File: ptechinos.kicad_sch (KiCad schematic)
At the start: 76 parts, among them J1 B+, J2 Battery, J3 B-, J4 TRRS, J5 Trackpad FPC, J6 OLED, J7 Pogo, SW1 SW_Power, SW2 Reset, U1 ProMicro

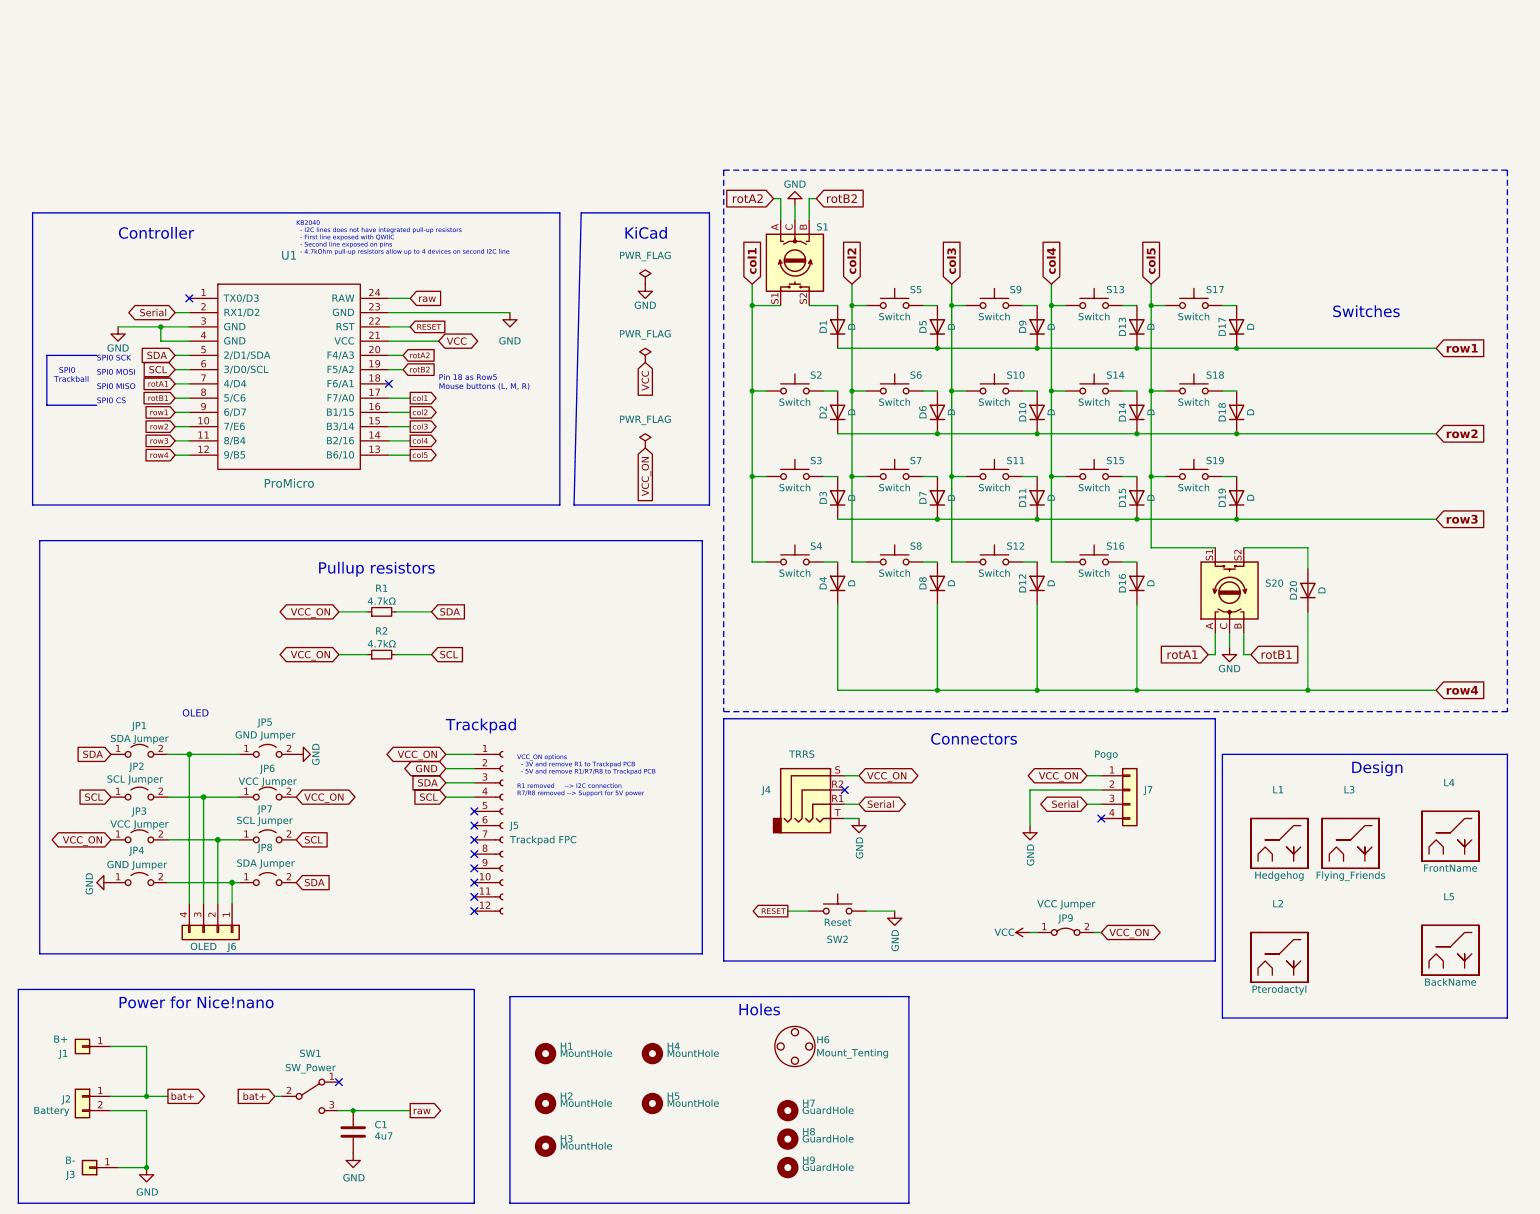
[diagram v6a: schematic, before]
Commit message: ✨ ♻️ - Add footprint for pogo connectors. Add SPI header pins 1.27mm pitch (used for trackball component). Update I2C resistors position (now below the MCU board on the other side). Replace reset switch with a smaller one and put it below the pogo connector (solder on the opposite side). Rename VCC / VCC_ON to 3.3V to make it more explicit about the voltage used by the RP2040 (does not break compatibility with EliteC like board). Remove VCC_ON altogether to make routing cleaner / easier.
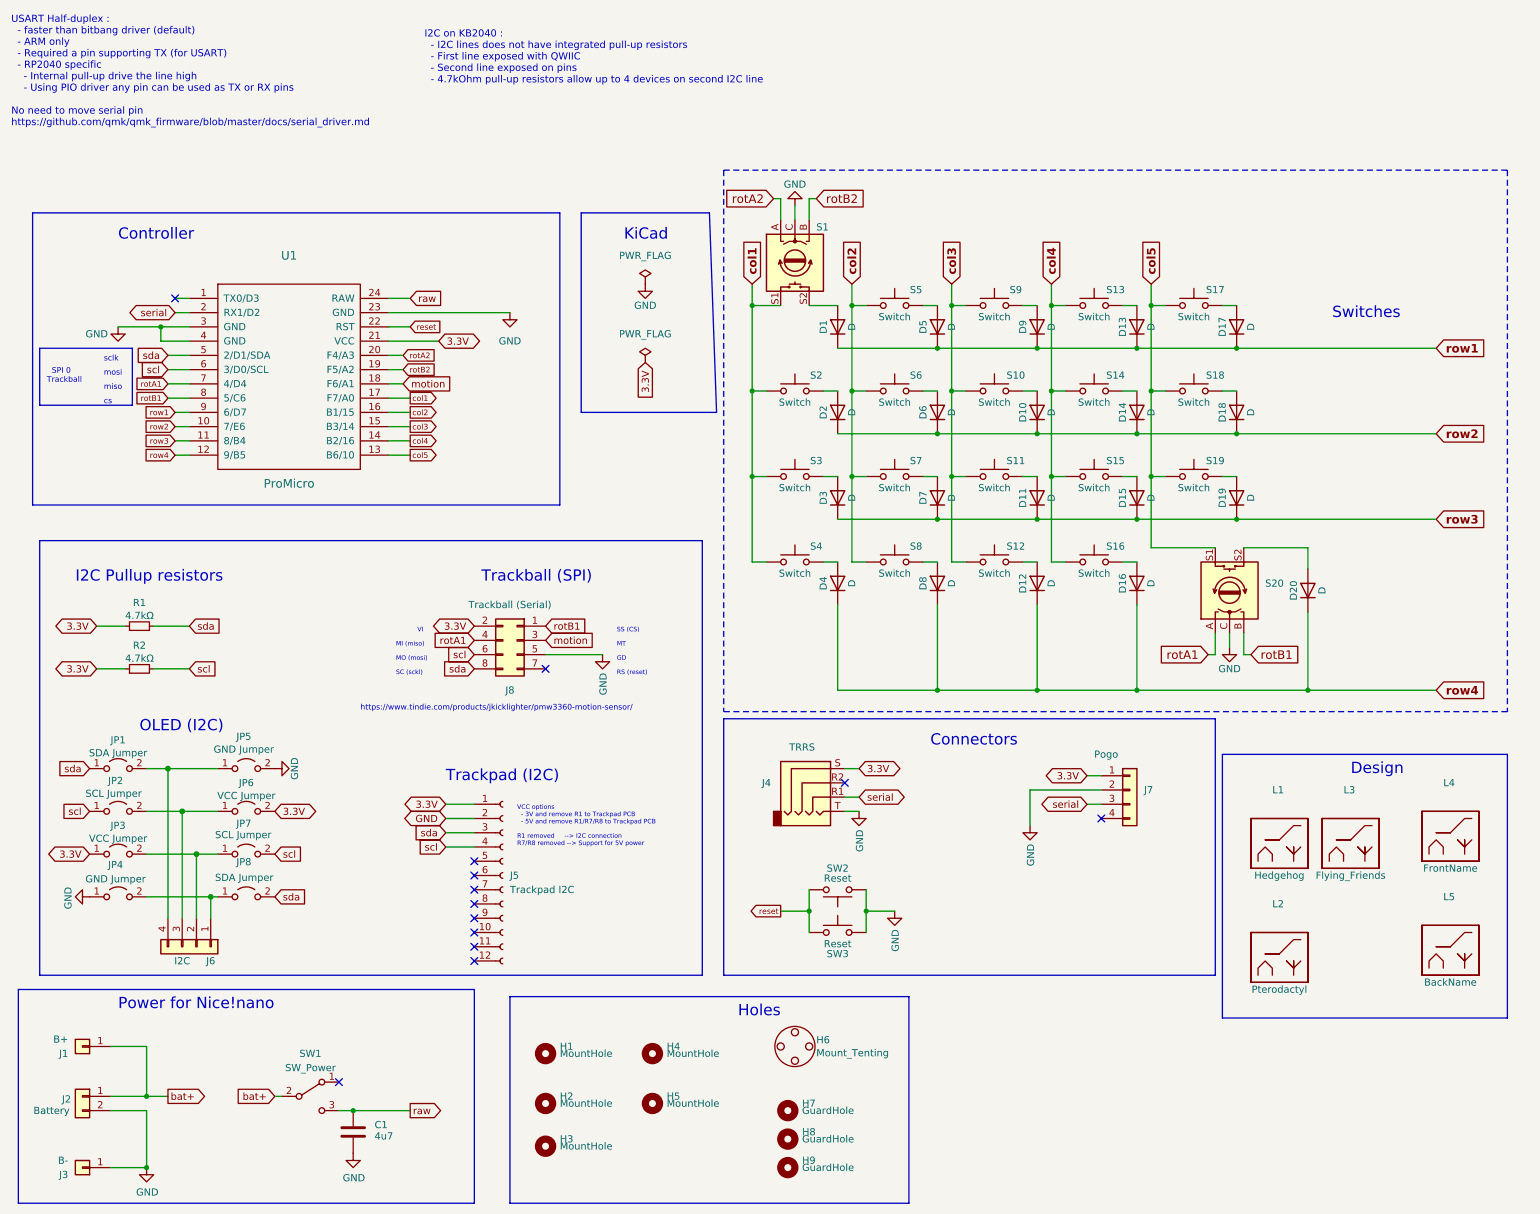
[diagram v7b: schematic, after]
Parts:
- removed JP9: VCC Jumper, Jumper:SolderJumper-2_P1.3mm_Bridged_RoundedPad1.0x1.5mm, symbol Jumper:Jumper_2_Bridged
- added J8: Trackball (Serial), Connector_PinHeader_1.27mm:PinHeader_2x04_P1.27mm_Horizontal, symbol Connector_Generic:Conn_02x04_Odd_Even
- added SW3: Reset, ptechinos:SW_SKRKAEE020_ALPS, symbol Switch:SW_Push
- J1, J3: footprint ptechinos:1pin_conn -> ptechinos:PinHeader_1x01
- J5: value Trackpad FPC -> Trackpad I2C
- J6: value OLED -> I2C
- J7: footprint ptechinos:PinSocket_1x04_P2.54mm_Vertical -> Connector_PinHeader_2.54mm:PinHeader_1x04_P2.54mm_Vertical
- SW2: footprint ptechinos:TACT_SWITCH_TVBP06 -> ptechinos:SW_SKRKAEE020_ALPS
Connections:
- net VCC_ON is gone; now on net 3.3V: J4.S, J5.1 (Pin_1), J7.1 (Pin_1), JP3.1 (A), JP6.2 (B), R1.1, R2.1
- net GND: now also SW2.1, J8.5 (Pin_5), SW3.2; no longer SW2.2
- net rotA1: now also J8.4 (Pin_4)
- net rotB1: now also J8.1 (Pin_1)
- net motion: now reaches U1.18 (F6/A1)
- net motion: now also J8.3 (Pin_3)
- net RESET renamed reset
- net reset: now also SW2.2, SW3.1; no longer SW2.1
- net SCL renamed scl
- net scl: now also J8.6 (Pin_6)
- net SDA renamed sda
- net sda: now also J8.8 (Pin_8)
- net Serial renamed serial
- net VCC renamed 3.3V
- net 3.3V: now also J8.2 (Pin_2)
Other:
- note added: "GD"
- note added: "I2C Pullup resistors"
- note added: "I2C on KB2040 : - I2C lines does not have integrated pull-up resistors - First line exposed with QWIIC - Second line exposed on pins - 4.7kOhm pull-up resistors allow up to 4 devices on second I2C line"
- note added: "MI (miso)"
- note added: "MO (mosi)"
- note added: "MT"
- note added: "OLED (I2C)"
- note added: "RS (reset)"
- note added: "SC (sckl)"
- note added: "SPI 0 Trackball"
- note added: "SS (CS)"
- note added: "Trackball (SPI)"
- note added: "Trackpad (I2C)"
- note added: "USART Half-duplex : - faster than bitbang driver (default) - ARM only - Required a pin supporting TX (for USART) - RP2040 specific - Internal pull-up drive the line high - Using PIO driver any pin can be used as TX or RX pins No need to move serial pin https://github.com/qmk/qmk_firmware/blob/master/docs/serial_driver.md"
- note added: "VCC options - 3V and remove R1 to Trackpad PCB - 5V and remove R1/R7/R8 to Trackpad PCB R1 removed --> I2C connection R7/R8 removed --> Support for 5V power"
- note added: "VI"
- note added: "cs"
- note added: "https://www.tindie.com/products/jkicklighter/pmw3360-motion-sensor/"
- note added: "miso"
- note added: "mosi"
- note added: "sclk"
- note removed: "KB2040 - I2C lines does not have integrated pull-up resistors - First line exposed with QWIIC - Second line exposed on pins - 4.7kOhm pull-up resistors allow up to 4 devices on second I2C line"
- note removed: "OLED"
- note removed: "Pin 18 as Row5 Mouse buttons (L, M, R)"
- note removed: "Pullup resistors"
- note removed: "SPI0 CS"
- note removed: "SPI0 MISO"
- note removed: "SPI0 MOSI"
- note removed: "SPI0 SCK"
- note removed: "SPI0 Trackball"
- note removed: "Trackpad"
- note removed: "VCC_ON options - 3V and remove R1 to Trackpad PCB - 5V and remove R1/R7/R8 to Trackpad PCB R1 removed --> I2C connection R7/R8 removed --> Support for 5V power"
- moved on the sheet: J3, J4, J5, J6, JP1, JP2, JP3, JP4, JP5, JP6, JP7, JP8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

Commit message: ♻️ 💄 - Remove redundant header pins (battery). Adjust SPI headers to let enough place for horizontal ones. Clean schematics and make some space to add notes about SPI, I2C, USART Half-duplex.
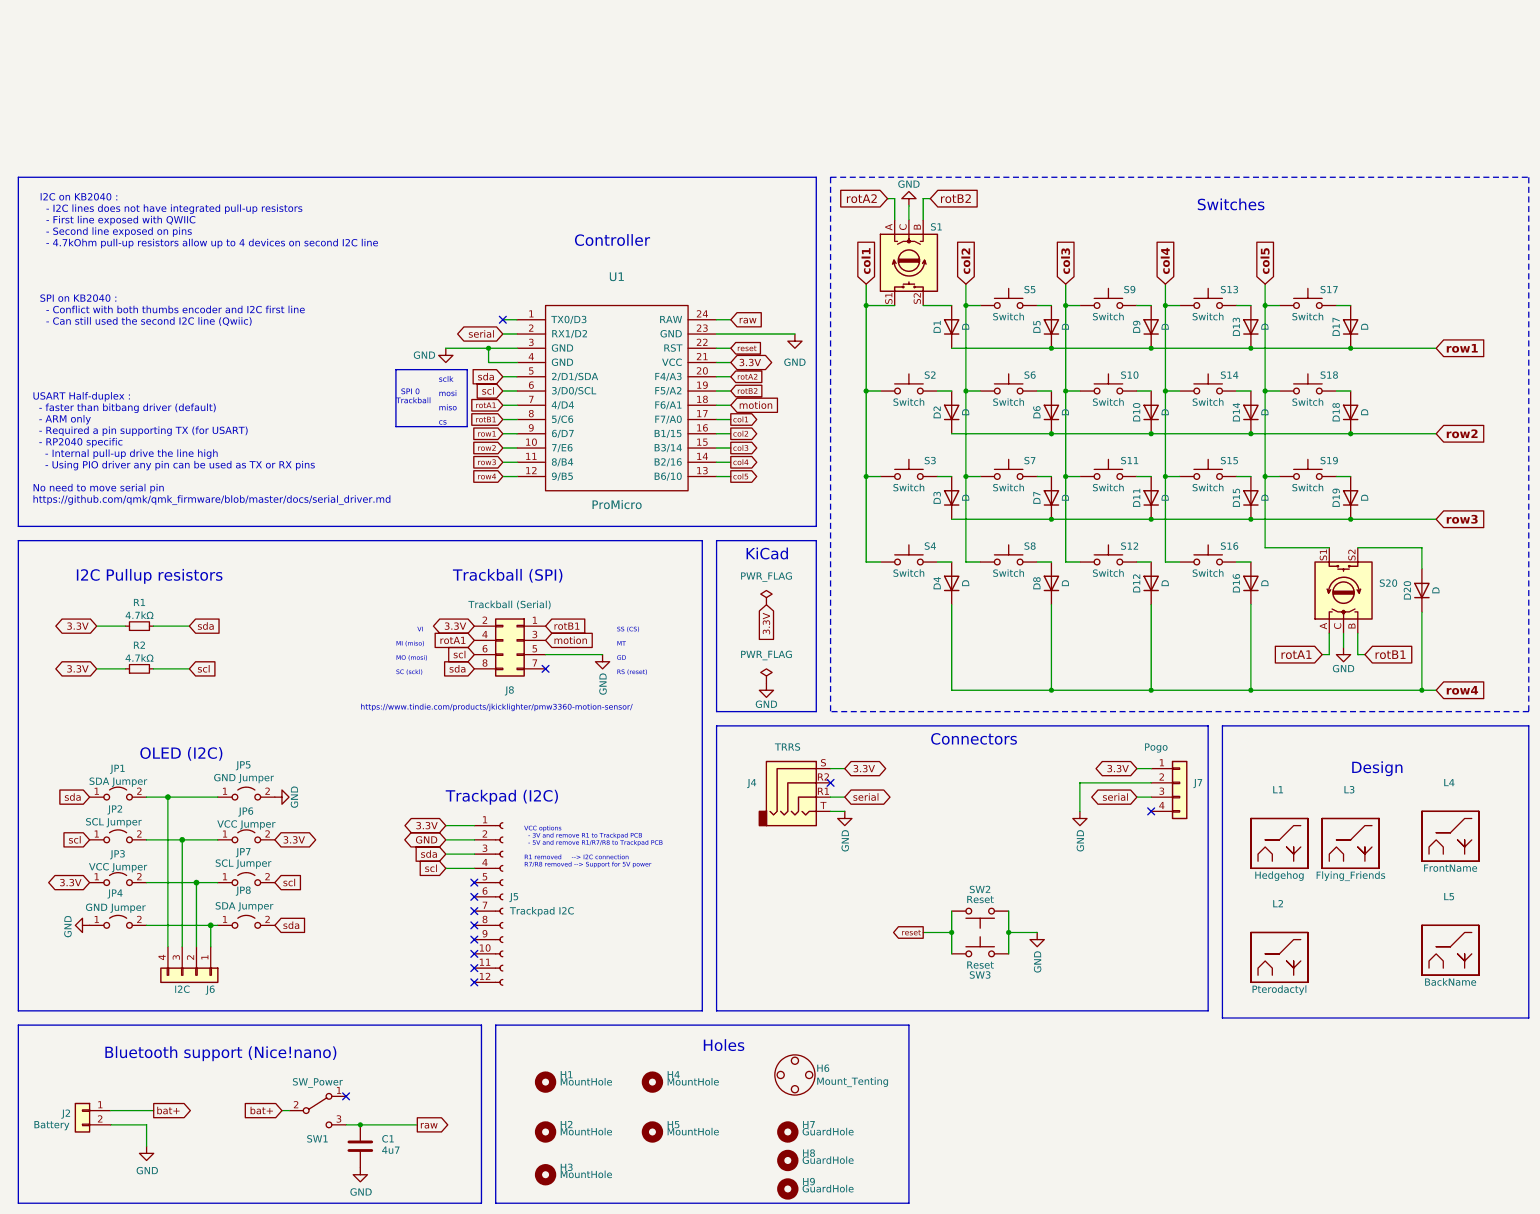
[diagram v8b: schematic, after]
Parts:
- removed J1: B+, ptechinos:PinHeader_1x01, symbol Connector_Generic:Conn_01x01
- removed J3: B-, ptechinos:PinHeader_1x01, symbol Connector_Generic:Conn_01x01
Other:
- note added: "Bluetooth support (Nice!nano)"
- note added: "SPI on KB2040 : - Conflict with both thumbs encoder and I2C first line - Can still used the second I2C line (Qwiic)"
- note removed: "Power for Nice!nano"
- moved on the sheet: C1, D1, D10, D11, D12, D13, D14, D15, D16, D17, D18, D19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
